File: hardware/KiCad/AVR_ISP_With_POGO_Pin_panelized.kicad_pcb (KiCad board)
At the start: 2 copper layers, 93.6 x 85.5 mm, 521 parts, among them P1 75869-131LF, P2 P50-B1

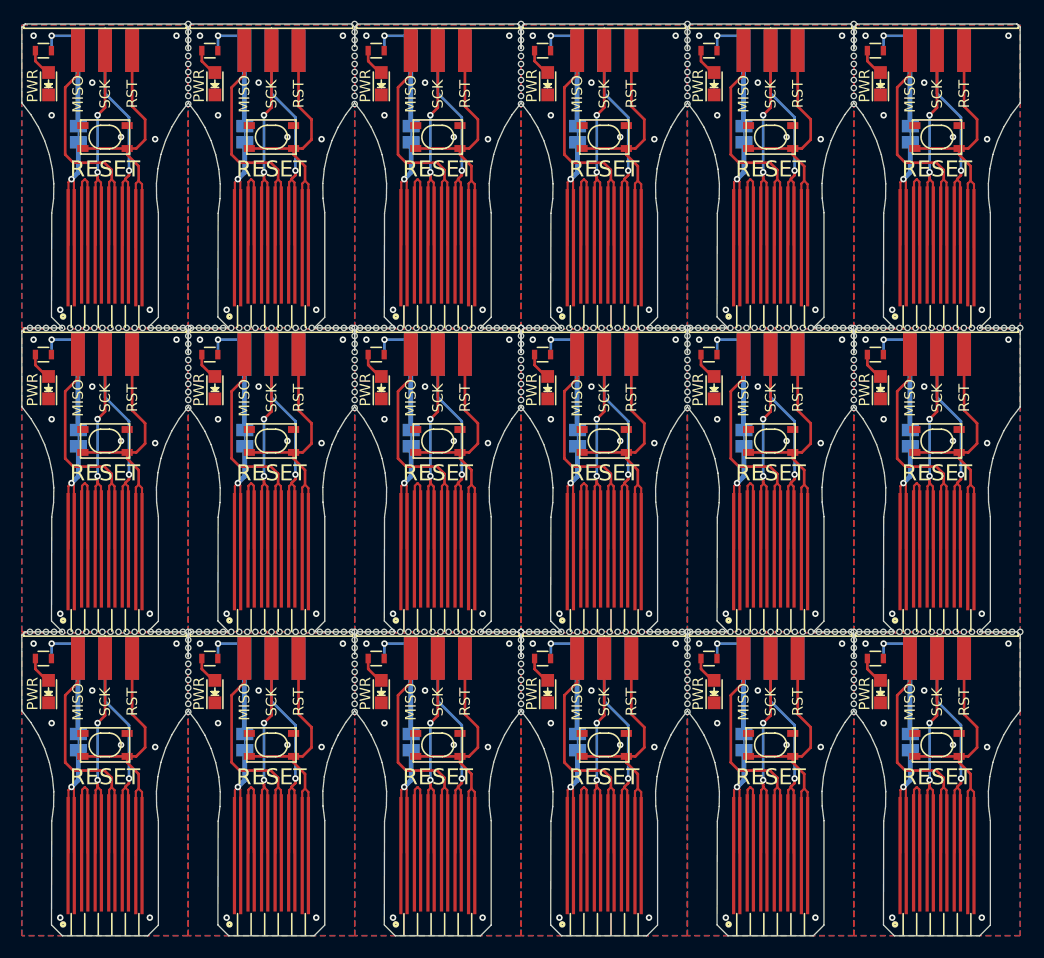
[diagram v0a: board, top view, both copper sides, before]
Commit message: Repanelized, reverted to V-Cut lines
Mousebites dont do the job probably the rest also NOT
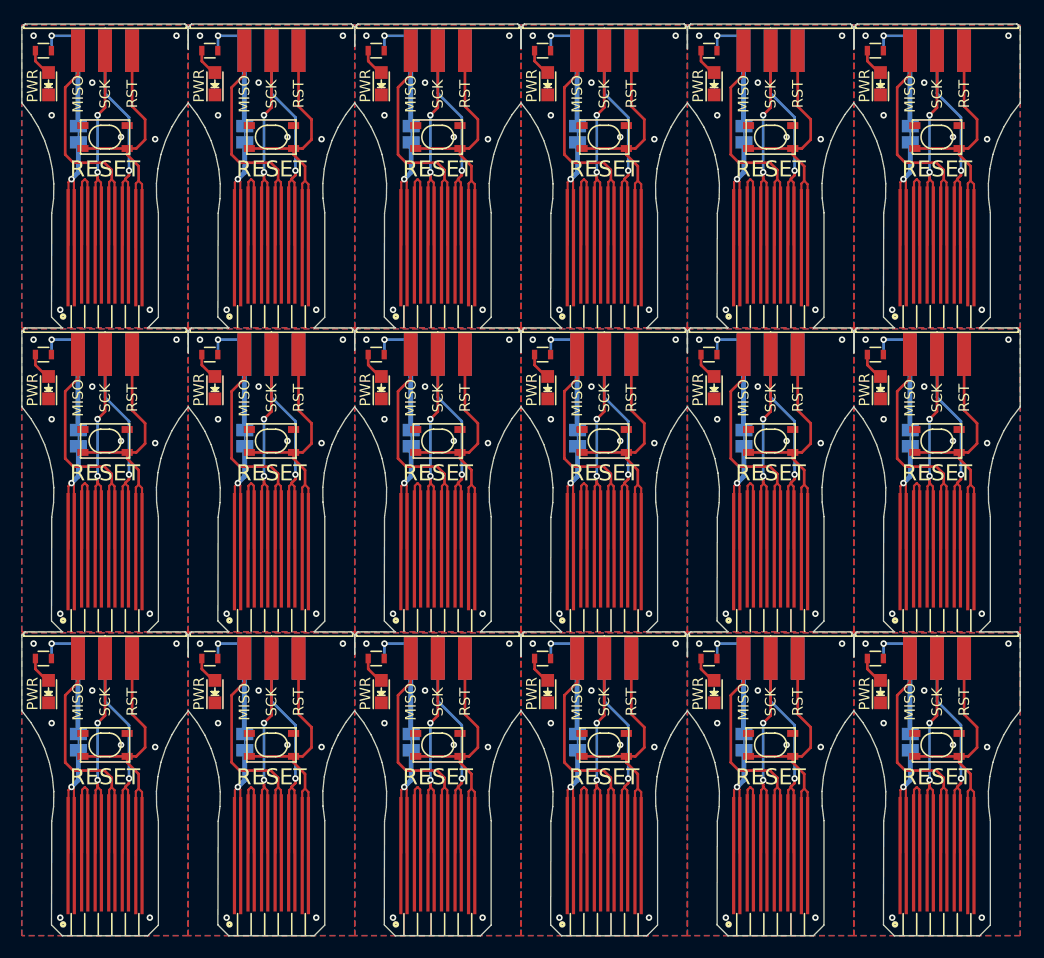
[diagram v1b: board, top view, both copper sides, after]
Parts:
- removed the D1 at (130.5, 84.1)
- removed the JP1 at (70.9, 117.3)
- removed the P1 at (89.0, 81.0)
- removed the P1 at (120.2, 109.5)
- removed the P2 at (135.8, 99.2)
- removed the R1 at (83.2, 109.5)
- removed REF** (x405): NPTH, NPTH
- removed the S1 at (135.8, 117.6)
- removed the S1 at (104.6, 89.1)
- D1: renamed from REF**; value NPTH -> PWR; footprint NPTH -> footprints:LED_0805
- JP1: renamed from REF**; value NPTH -> Jumper_NO_Small; footprint NPTH -> footprints:SJ_OPEN; moved to B.Cu
- P1 (x2): renamed from REF**; value NPTH -> 75869-131LF; footprint NPTH -> footprints:2x6_idc_box_header_pcb_side_mount
- P2: renamed from REF**; value NPTH -> P50-B1; footprint NPTH -> footprints:POGO_ISP
- R1: renamed from REF**; value NPTH -> 470R; footprint NPTH -> footprints:R_0603
- S1 (x2): renamed from REF**; value NPTH -> PTS810 SJM 250 SMTR LFS; footprint NPTH -> footprints:PTS810_tactile_push_button
- moved S1 39.7 mm to (135.8, 117.6), turned to 270 degrees
- moved P1 39.0 mm to (120.2, 109.5)
- moved R1 35.6 mm to (83.2, 109.5), turned to 180 degrees
- moved P1 32.3 mm to (89.0, 81.0)
- moved S1 25.2 mm to (104.6, 89.1), turned to 270 degrees
- moved JP1 22.4 mm to (70.9, 117.3), turned to 90 degrees
- moved P2 20.8 mm to (135.8, 99.2), turned to 180 degrees
- moved D1 5.62 mm to (130.5, 84.1), turned to 90 degrees
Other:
- board text added: "V-CUT"
